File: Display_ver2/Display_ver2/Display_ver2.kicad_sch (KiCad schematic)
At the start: 2 parts, among them J1 toDisplay, J2 fromCPU

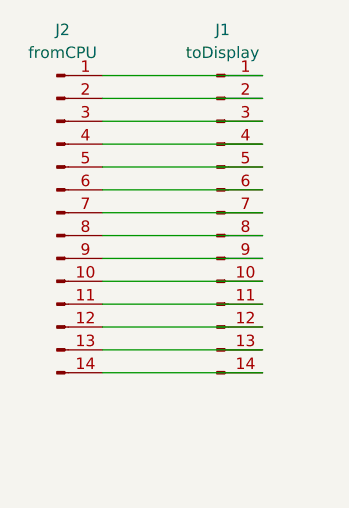
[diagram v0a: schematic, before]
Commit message: display-main接続
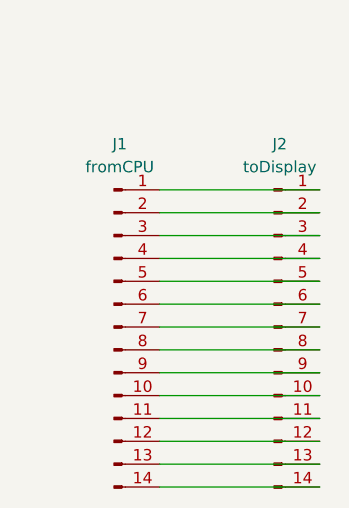
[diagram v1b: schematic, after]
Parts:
- J1: value toDisplay -> fromCPU; footprint Connector_PinSocket_2.54mm:PinSocket_1x14_P2.54mm_Vertical -> Connector_JST:JST_XH_S14B-XH-A-1_1x14_P2.50mm_Horizontal
- J2: value fromCPU -> toDisplay; footprint Connector_JST:JST_ZE_S14B-ZESK-2D_1x14_P1.50mm_Horizontal -> Connector_PinSocket_2.54mm:PinSocket_1x14_P2.54mm_Vertical
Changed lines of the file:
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@@
 (kicad_sch (version 20230121) (generator eeschema)
   (paper "A4")
-  (wire (pts (xy 139.7 76.2) (xy 121.92 76.2))
+  (wire (pts (xy 146.05 104.14) (xy 128.27 104.14))
     (stroke (width 0) (type default))
   )
-  (wire (pts (xy 139.7 83.82) (xy 121.92 83.82))
+  (wire (pts (xy 146.05 106.68) (xy 128.27 106.68))
     (stroke (width 0) (type default))
   )
-  (wire (pts (xy 139.7 86.36) (xy 121.92 86.36))
+  (wire (pts (xy 146.05 78.74) (xy 128.27 78.74))
     (stroke (width 0) (type default))
   )
-  (wire (pts (xy 139.7 81.28) (xy 121.92 81.28))
+  (wire (pts (xy 146.05 81.28) (xy 128.27 81.28))
     (stroke (width 0) (type default))
   )
-  (wire (pts (xy 139.7 93.98) (xy 121.92 93.98))
+  (wire (pts (xy 146.05 99.06) (xy 128.27 99.06))
     (stroke (width 0) (type default))
   )
-  (wire (pts (xy 139.7 78.74) (xy 121.92 78.74))
+  (wire (pts (xy 146.05 111.76) (xy 128.27 111.76))
     (stroke (width 0) (type default))
   )
-  (wire (pts (xy 139.7 66.04) (xy 121.92 66.04))
+  (wire (pts (xy 146.05 93.98) (xy 128.27 93.98))
     (stroke (width 0) (type default))
   )
-  (wire (pts (xy 139.7 68.58) (xy 121.92 68.58))
+  (wire (pts (xy 146.05 101.6) (xy 128.27 101.6))
     (stroke (width 0) (type default))
   )
-  (wire (pts (xy 139.7 73.66) (xy 121.92 73.66))
+  (wire (pts (xy 146.05 91.44) (xy 128.27 91.44))
     (stroke (width 0) (type default))
   )
-  (wire (pts (xy 139.7 88.9) (xy 121.92 88.9))
+  (wire (pts (xy 146.05 96.52) (xy 128.27 96.52))
     (stroke (width 0) (type default))
   )
-  (wire (pts (xy 139.7 96.52) (xy 121.92 96.52))
+  (wire (pts (xy 146.05 109.22) (xy 128.27 109.22))
     (stroke (width 0) (type default))
   )
-  (wire (pts (xy 139.7 99.06) (xy 121.92 99.06))
+  (wire (pts (xy 146.05 86.36) (xy 128.27 86.36))
     (stroke (width 0) (type default))
   )
-  (wire (pts (xy 139.7 91.44) (xy 121.92 91.44))
+  (wire (pts (xy 146.05 88.9) (xy 128.27 88.9))
     (stroke (width 0) (type default))
   )
-  (wire (pts (xy 139.7 71.12) (xy 121.92 71.12))
+  (wire (pts (xy 146.05 83.82) (xy 128.27 83.82))
     (stroke (width 0) (type default))
   )
-  (symbol (lib_id "Connector:Conn_01x14_Pin") (at 134.62 81.28 0) (unit 1)
+  (symbol (lib_id "Connector:Conn_01x14_Pin") (at 123.19 93.98 0) (unit 1)
     (in_bom yes) (on_board yes) (dnp no) (fields_autoplaced)
-    (property "Reference" "J1" (at 135.255 60.96 0)
+    (property "Reference" "J1" (at 123.825 73.66 0)
       (effects (font (face "Calibri") (size 1.27 1.27)))
     )
-    (property "Value" "toDisplay" (at 135.255 63.5 0)
+    (property "Value" "fromCPU" (at 123.825 76.2 0)
       (effects (font (face "Calibri") (size 1.27 1.27)))
     )
-    (property "Footprint" "Connector_PinSocket_2.54mm:PinSocket_1x14_P2.54mm_Vertical" (at 134.62 81.28 0)
+    (property "Footprint" "Connector_JST:JST_XH_S14B-XH-A-1_1x14_P2.50mm_Horizontal" (at 123.19 93.98 0)
       (effects (font (size 1.27 1.27)) hide)
     )
-    (property "Datasheet" "~" (at 134.62 81.28 0)
+    (property "Datasheet" "~" (at 123.19 93.98 0)
       (effects (font (size 1.27 1.27)) hide)
     )
@@
     (pin "9")
     (instances
+      (project "Display_ver2"
+        (path "/d642f31c-4d5f-443a-ae08-789aa9345850"
+          (reference "J1") (unit 1)
+        )
+      )
       (project "Display"
         (path "/d8d08799-c793-4824-8077-a92339585114"
-          (reference "J1") (unit 1)
+          (reference "J2") (unit 1)
         )
       )
     )
   )
-  (symbol (lib_id "Connector:Conn_01x14_Pin") (at 116.84 81.28 0) (unit 1)
+  (symbol (lib_id "Connector:Conn_01x14_Pin") (at 140.97 93.98 0) (unit 1)
     (in_bom yes) (on_board yes) (dnp no) (fields_autoplaced)
-    (property "Reference" "J2" (at 117.475 60.96 0)
+    (property "Reference" "J2" (at 141.605 73.66 0)
       (effects (font (face "Calibri") (size 1.27 1.27)))
     )
-    (property "Value" "fromCPU" (at 117.475 63.5 0)
+    (property "Value" "toDisplay" (at 141.605 76.2 0)
       (effects (font (face "Calibri") (size 1.27 1.27)))
     )
-    (property "Footprint" "Connector_JST:JST_ZE_S14B-ZESK-2D_1x14_P1.50mm_Horizontal" (at 116.84 81.28 0)
+    (property "Footprint" "Connector_PinSocket_2.54mm:PinSocket_1x14_P2.54mm_Vertical" (at 140.97 93.98 0)
       (effects (font (size 1.27 1.27)) hide)
     )
-    (property "Datasheet" "~" (at 116.84 81.28 0)
+    (property "Datasheet" "~" (at 140.97 93.98 0)
       (effects (font (size 1.27 1.27)) hide)
     )
@@
     (pin "9")
     (instances
-      (project "Display"
-        (path "/d8d08799-c793-4824-8077-a92339585114"
+      (project "Display_ver2"
+        (path "/d642f31c-4d5f-443a-ae08-789aa9345850"
           (reference "J2") (unit 1)
         )
       )
+      (project "Display"
+        (path "/d8d08799-c793-4824-8077-a92339585114"
+          (reference "J1") (unit 1)
+        )
+      )
